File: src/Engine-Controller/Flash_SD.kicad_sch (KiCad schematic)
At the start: 7 parts, among them P6 Micro_SD_Card, U5 SST25VF040B-50-4I-S2AE-T

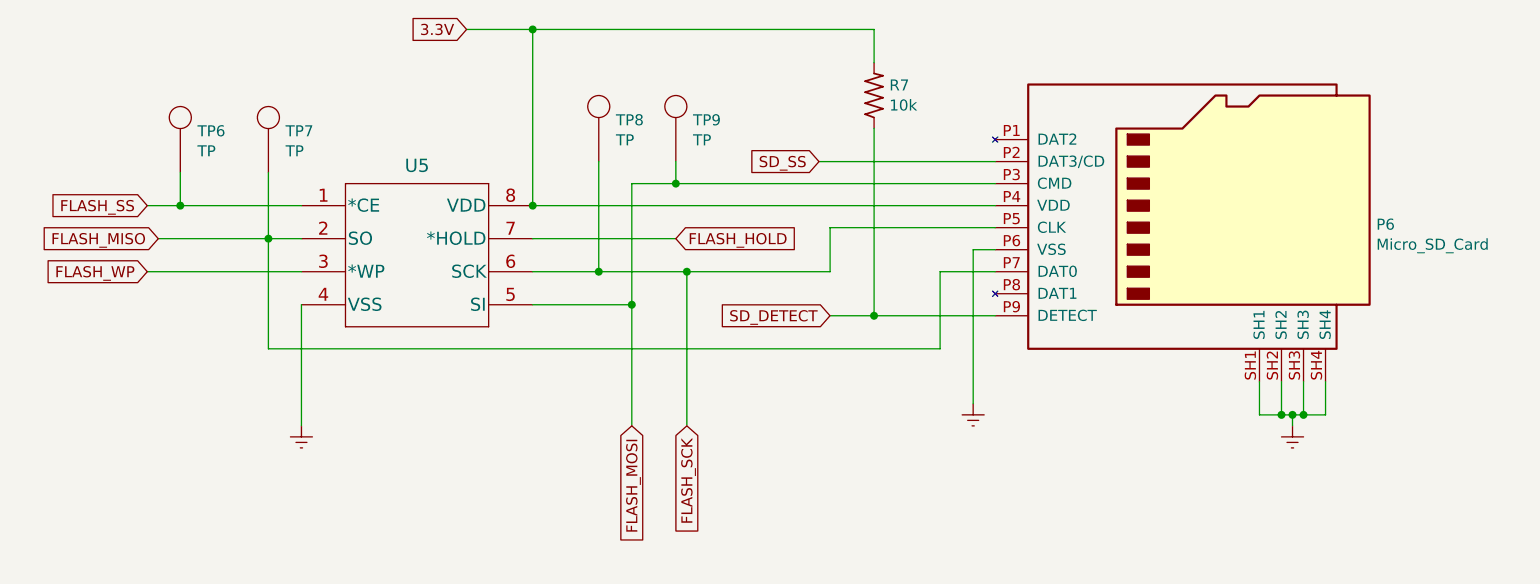
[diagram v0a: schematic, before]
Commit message: Removed misc elements from connectors sheet
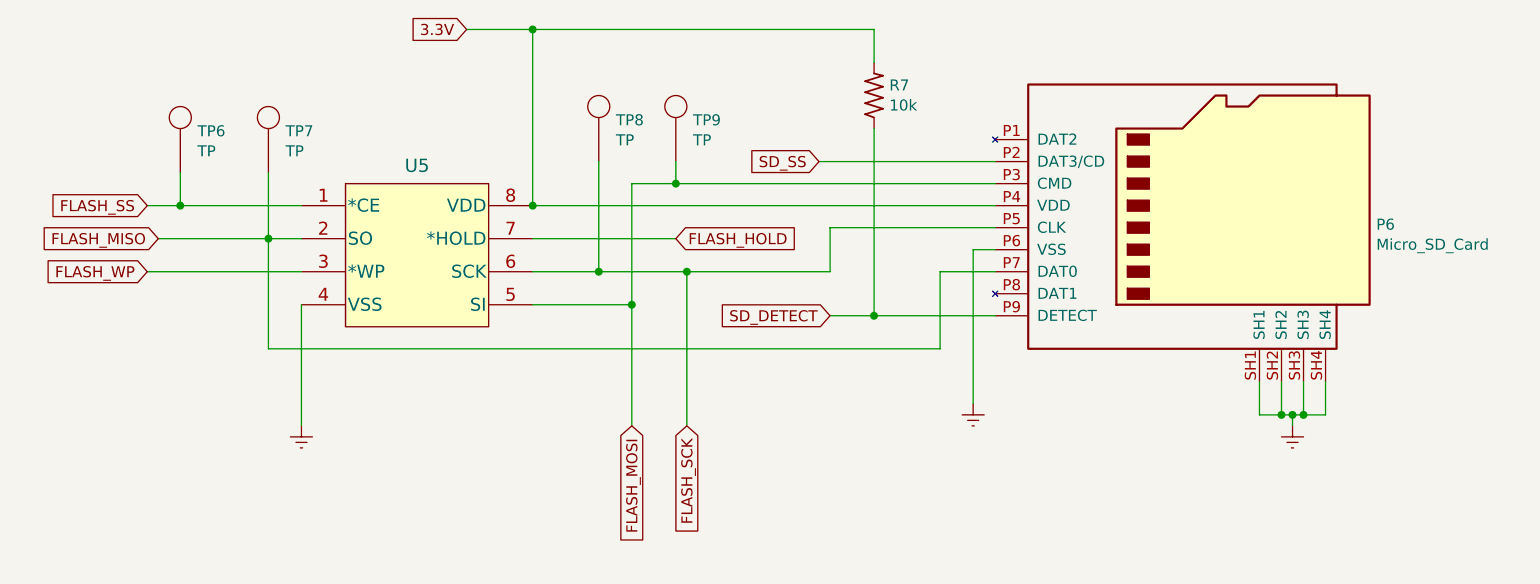
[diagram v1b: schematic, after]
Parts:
- U5: footprint Engine-Controller:SST25VF040B-50-4I-S2AE-T -> SOIC8_S2A_SST_MCH
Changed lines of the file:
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@@
       (effects (font (size 1.524 1.524)) hide)
     )
-    (property "Footprint" "Engine-Controller:SST25VF040B-50-4I-S2AE-T" (id 2) (at 115.57 116.84 0)
+    (property "Footprint" "SOIC8_S2A_SST_MCH" (id 2) (at 115.57 116.84 0)
       (effects (font (size 1.524 1.524)) hide)
     )
